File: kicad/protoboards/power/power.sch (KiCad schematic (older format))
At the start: 40 parts, among them J1 PCIEPWR, U18 IR3895, U20 MCP16321

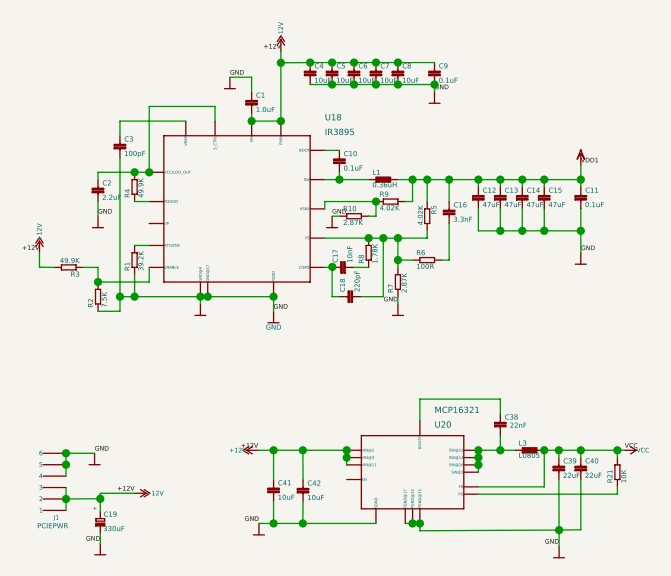
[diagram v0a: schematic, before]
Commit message: update test power board
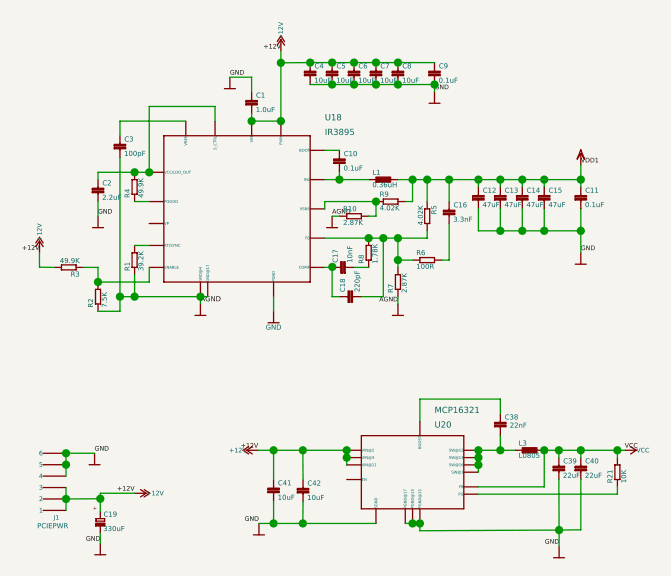
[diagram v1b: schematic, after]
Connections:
- net GND: no longer C3.2, R1.1, R10.1, R2.1, R7.1, U18.11 (PGND), U18.17 (GND@17), U18.4 (GND@4)
- new net AGND: C3.2, R1.1, R10.1, R2.1, R7.1, U18.17 (GND@17), U18.4 (GND@4)
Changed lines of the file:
@@
-EESchema Schematic File Version 2  date Wed 08 May 2013 10:32:12 AM ICT
-LIBS:asic-v1_-cache
+EESchema Schematic File Version 2  date Thu 09 May 2013 08:25:29 AM ICT
+LIBS:k16
 LIBS:power
 LIBS:device
@@
 Sheet 1 1
 Title "power.sch"
-Date "6 may 2013"
+Date "9 may 2013"
 Rev ""
 Comp ""
@@
 Connection ~ 9225 4527
 Wire Wire Line
-	7561 4815 8233 4815
-Wire Wire Line
-	7913 4847 7913 4815
+	7913 4815 7913 4847
 Wire Wire Line
 	7561 4207 7561 4879
@@
 Wire Wire Line
 	7561 4879 7465 4879
-Wire Wire Line
-	8233 4815 8233 4879
 Connection ~ 7913 4815
 Connection ~ 7625 4815
 Connection ~ 7561 4815
-Connection ~ 7945 4815
-Connection ~ 8233 4815
 Wire Wire Line
 	8361 5807 8362 5712
@@
 Text Label 9482 5907 2    20   ~ 0
 GND
-Text Label 8233 4879 0    20   ~ 0
-GND
 Text Label 7475 5894 2    20   ~ 0
 GND
@@
 GND
 Text Label 8777 4847 2    20   ~ 0
-GND
+AGND
 $Comp
 L VDD1 #VDD0101
@@
 GND
 Text Label 8489 4463 0    20   ~ 0
-GND
+AGND
 Text Label 8042 3855 0    20   ~ 0
 GND
+Wire Wire Line
+	7561 4815 7945 4815
+Wire Wire Line
+	8233 4815 8233 4879
+Text Label 7913 4847 0    22   ~ 0
+AGND
 $EndSCHEMATC
